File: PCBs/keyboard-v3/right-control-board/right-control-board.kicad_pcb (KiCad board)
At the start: 2 copper layers, 105 x 44 mm, 0 parts

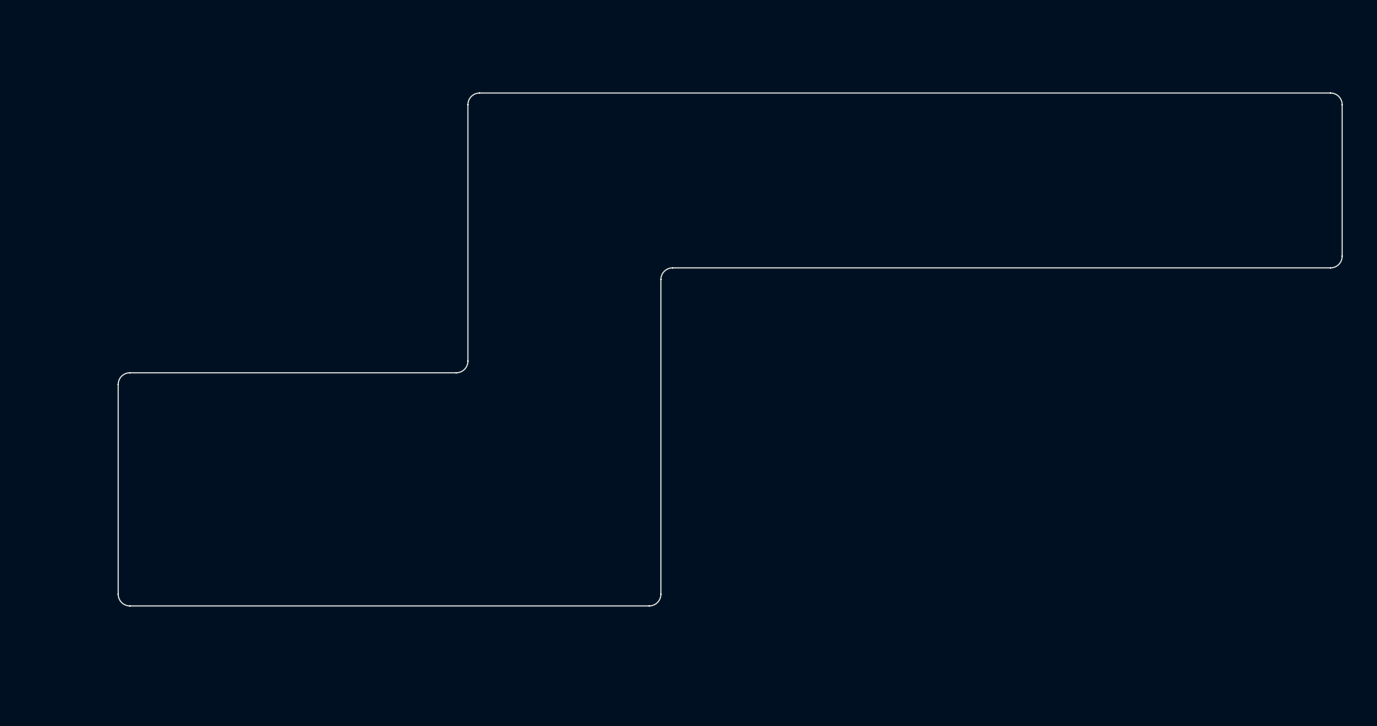
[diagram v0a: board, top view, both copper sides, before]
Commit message: Updated right-control-board layout
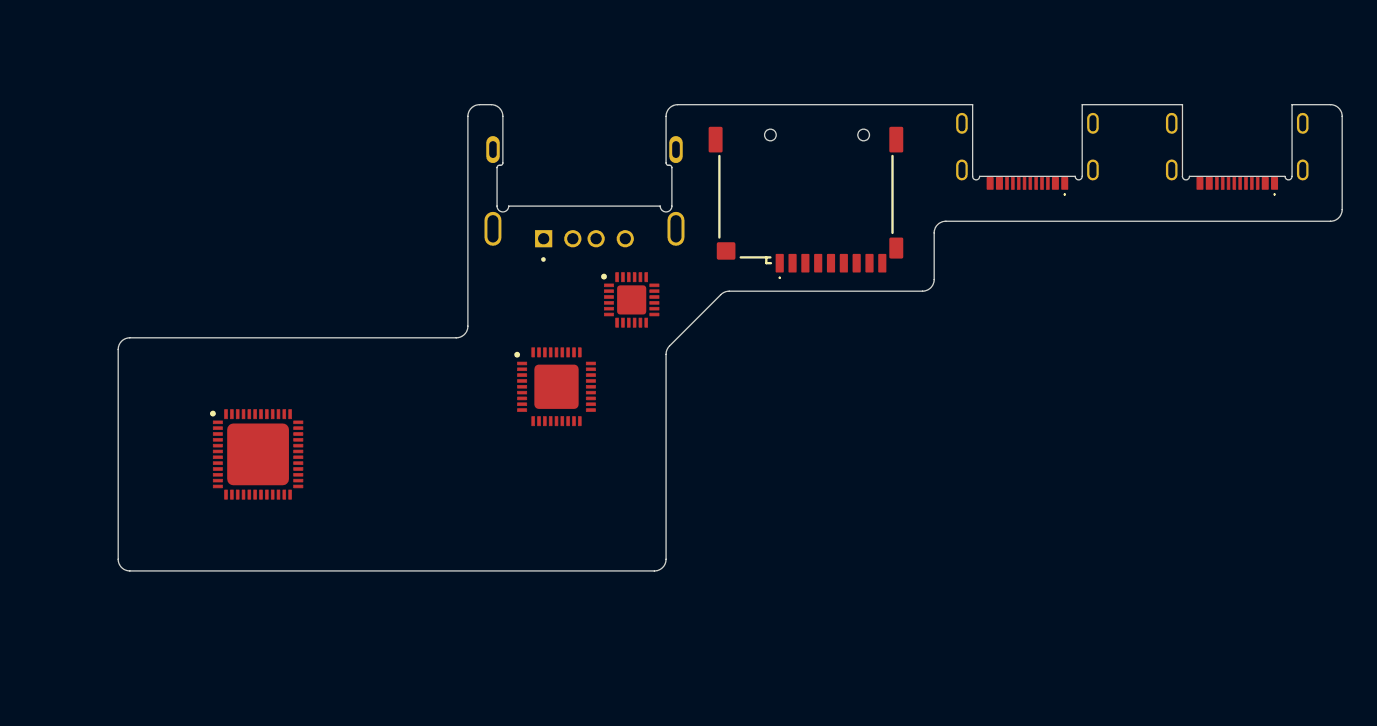
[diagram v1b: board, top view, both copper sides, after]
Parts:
- added J101: USB4510-03-1-A, project_footprints:USB4510031A, F.Cu at (196.0, 78.0)
- added J102: USB4510-03-1-A, project_footprints:USB4510031A, F.Cu at (178.0, 78.0)
- added J103: GSB12J21C1EU, project_footprints:GSB12J21C1EU, F.Cu at (140.0, 79.0)
- added J105: MSD-1-A, project_footprints:MSD1A, F.Cu at (159.0, 84.5)
- added U101: USB2534-1080AEN, project_footprints:QFN50P600X600X100-37N-D, F.Cu at (137.6, 102.2)
- added U102: STM32G0C1CEUx, project_footprints:QFN50P700X700X60-49N-D, F.Cu at (112.0, 108.0)
- added U103: GL835, project_footprints:QFN50P400X400X100-25N-D, F.Cu at (144.1, 94.8)
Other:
- board size 105 x 44 mm -> 105 x 40 mm

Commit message: Right control board schematic almost done
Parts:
- added C101: 1u, project_footprints:C_0402, F.Cu at (173.8, 102.2)
- added C102: 10p, project_footprints:C_0402, F.Cu at (173.8, 104.2)
- added C103: 10p, project_footprints:C_0402, F.Cu at (173.8, 106.1)
- added C105: 1u, project_footprints:C_0402, F.Cu at (173.8, 108.1)
- added C106: 100n, project_footprints:C_0402, F.Cu at (173.8, 110.1)
- added C109: 100n, project_footprints:C_0402, F.Cu at (163.3, 116.4)
- added C110: 1u, project_footprints:C_0402, F.Cu at (163.3, 118.4)
- added C111: 4u7, project_footprints:C_0402, F.Cu at (163.3, 120.4)
- added C201: 4u7, project_footprints:C_0402, F.Cu at (184.4, 114.0)
- added C202: 4u7, project_footprints:C_0402, F.Cu at (184.4, 116.0)
- added C203: 22p, project_footprints:C_0402, F.Cu at (184.4, 118.0)
- added C204: 4u7, project_footprints:C_0402, F.Cu at (184.4, 119.9)
- added C205: 4u7, project_footprints:C_0402, F.Cu at (184.4, 121.9)
- added C206: 4u7, project_footprints:C_0402, F.Cu at (184.4, 123.9)
- added C301: 100n, project_footprints:C_0402, F.Cu at (173.8, 114.0)
- added C302: 4u7, project_footprints:C_0402, F.Cu at (173.8, 116.0)
- added C303: 4u7, project_footprints:C_0402, F.Cu at (173.8, 118.0)
- added C304: 100n, project_footprints:C_0402, F.Cu at (176.7, 114.0)
- added C305: 4u7, project_footprints:C_0402, F.Cu at (176.7, 116.0)
- added C306: 100n, project_footprints:C_0402, F.Cu at (176.7, 118.0)
- added C307: 100n, project_footprints:C_0402, F.Cu at (179.6, 114.0)
- added C308: 4u7, project_footprints:C_0402, F.Cu at (179.6, 116.0)
- added C309: 4u7, project_footprints:C_0402, F.Cu at (179.6, 118.0)
- added FL301: EMIF06-MSD02N16, project_footprints:EMIF06MSD02N16, F.Cu at (176.5, 121.1)
- added J501: Conn_02x08_Odd_Even, Connector_PinSocket_1.27mm:PinSocket_2x08_P1.27mm_Horizontal, F.Cu at (97.8, 103.5)
- added L201: 78438313015, project_footprints:L_Wurth_WE-MAIA-1610, F.Cu at (187.6, 122.1)
- added R101: 10k, project_footprints:R_0402, F.Cu at (166.2, 116.4)
- added R102: 10k, project_footprints:R_0402, F.Cu at (166.2, 118.4)
- added R103: 12k, project_footprints:R_0402, F.Cu at (176.7, 102.2)
- added R104: 100k, project_footprints:R_0402, F.Cu at (176.7, 104.2)
- added R105: 47k, project_footprints:R_0402, F.Cu at (176.7, 106.2)
- added R108: 10k, project_footprints:R_0402, F.Cu at (176.7, 108.2)
- added R201: 5k1, project_footprints:R_0402, F.Cu at (170.2, 103.1)
- added R202: 5k1, project_footprints:R_0402, F.Cu at (170.2, 105.1)
- added R203: 5k1, project_footprints:R_0402, F.Cu at (170.2, 107.1)
- added R204: 5k1, project_footprints:R_0402, F.Cu at (170.2, 109.1)
- added R701: 820k, project_footprints:R_0402, F.Cu at (187.3, 114.0)
- added R702: 182k, project_footprints:R_0402, F.Cu at (187.3, 116.0)
- added U104: USBLC6-4SC6, Package_TO_SOT_SMD:SOT-23-6, F.Cu at (186.8, 103.6)
- added U201: USBLC6-4SC6, Package_TO_SOT_SMD:SOT-23-6, F.Cu at (186.8, 108.2)
- added U701: TPS62290TDRVRQ1, project_footprints:SON65P200X200X80-7N, F.Cu at (187.8, 118.8)
- added Y101: CX2016SA24000D0HLLG3, Crystal:Crystal_SMD_2016-4Pin_2.0x1.6mm, F.Cu at (180.2, 103.0)
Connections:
- J101 pad A1: Net-(J101-GND-PadA1) -> GND
- J101 pad A12: Net-(J101-GND-PadA1) -> GND
- J101 pad A4: Net-(J101-VBUS-PadA4) -> VBUS
- J101 pad A5: unconnected-(J101-CC1-PadA5) -> /USB Connectors/USB0_CC1
- J101 pad A6: Net-(J101-D+-PadA6) -> /USB Connectors/USB0.DP
- J101 pad A7: Net-(J101-D--PadA7) -> /USB Connectors/USB0.DN
- J101 pad A9: Net-(J101-VBUS-PadA4) -> VBUS
- J101 pad B5: unconnected-(J101-CC2-PadB5) -> /USB Connectors/USB0_CC2
- J101 pad B6: Net-(J101-D+-PadA6) -> /USB Connectors/USB0.DP
- J101 pad B7: Net-(J101-D--PadA7) -> /USB Connectors/USB0.DN
- J101 pad MH1: Net-(J101-PadMH1) -> GND
- J101 pad MH2: Net-(J101-PadMH1) -> GND
- J101 pad MH3: Net-(J101-PadMH1) -> GND
- J101 pad MH4: Net-(J101-PadMH1) -> GND
- J102 pad A1: Net-(J102-GND-PadA1) -> GND
- J102 pad A12: Net-(J102-GND-PadA1) -> GND
- J102 pad A4: Net-(J102-VBUS-PadA4) -> VBUS
- J102 pad A5: unconnected-(J102-CC1-PadA5) -> /USB Connectors/USB1_CC1
- J102 pad A6: Net-(J102-D+-PadA6) -> /USB Connectors/USB1.DP
- J102 pad A7: Net-(J102-D--PadA7) -> /USB Connectors/USB1.DN
- J102 pad A9: Net-(J102-VBUS-PadA4) -> VBUS
- J102 pad B5: unconnected-(J102-CC2-PadB5) -> /USB Connectors/USB1_CC2
- J102 pad B6: Net-(J102-D+-PadA6) -> /USB Connectors/USB1.DP
- J102 pad B7: Net-(J102-D--PadA7) -> /USB Connectors/USB1.DN
- J102 pad MH1: Net-(J102-PadMH1) -> GND
- J102 pad MH2: Net-(J102-PadMH1) -> GND
- J102 pad MH3: Net-(J102-PadMH1) -> GND
- J102 pad MH4: Net-(J102-PadMH1) -> GND
- J103 pad 1: unconnected-(J103-VCC-Pad1) -> VBUS
- J103 pad 2: unconnected-(J103-D--Pad2) -> /USB Connectors/USB2.DP
- J103 pad 3: unconnected-(J103-D+-Pad3) -> /USB Connectors/USB2.DN
- J103 pad 4: unconnected-(J103-GND-Pad4) -> GND
- J103 pad SH1: Net-(J103-SHIELD-PadSH1) -> GND
- J103 pad SH2: Net-(J103-SHIELD-PadSH1) -> GND
- J103 pad SH3: Net-(J103-SHIELD-PadSH1) -> GND
- J103 pad SH4: Net-(J103-SHIELD-PadSH1) -> GND
- J105 pad 1: unconnected-(J105-DAT2-Pad1) -> /SD Card/SD_D2_EX
- J105 pad 10: Net-(J105-SHIELD-Pad10) -> GND
- J105 pad 11: Net-(J105-SHIELD-Pad10) -> GND
- J105 pad 12: Net-(J105-SHIELD-Pad10) -> GND
- J105 pad 2: unconnected-(J105-CD/DAT3-Pad2) -> /SD Card/SD_D3_EX
- J105 pad 3: unconnected-(J105-CMD-Pad3) -> /SD Card/SD_CMD_EX
- J105 pad 4: unconnected-(J105-VDD-Pad4) -> /SD Card/SD_VCC
- J105 pad 5: unconnected-(J105-CLK-Pad5) -> /SD Card/SD_CLK_EX
- J105 pad 6: unconnected-(J105-VSS-Pad6) -> GND
- J105 pad 7: unconnected-(J105-DAT0-Pad7) -> /SD Card/SD_D0_EX
- J105 pad 8: unconnected-(J105-DAT1-Pad8) -> /SD Card/SD_D1_EX
- J105 pad 9: Net-(J105-SHIELD-Pad10) -> GND
- J105 pad CD: unconnected-(J105-PadCD) -> /SD Card/CD
- U101 pad 1: unconnected-(U101-SWAP_USBDN1_DM/PRT_DIS_M1-Pad1) -> /USB Connectors/USB1.DN
- U101 pad 10: unconnected-(U101-VDDA33_1-Pad10) -> +3V3
- U101 pad 14: unconnected-(U101-VDDCR12-Pad14) -> +1V2
- U101 pad 15: unconnected-(U101-VDD33_1-Pad15) -> +3V3
- U101 pad 2: unconnected-(U101-SWAP_USBDN1_DP/PRT_DIS_P1-Pad2) -> /USB Connectors/USB1.DP
- U101 pad 22: unconnected-(U101-SDA/SMBDATA/NON_REM1-Pad22) -> /MCU/SDA
- U101 pad 23: unconnected-(U101-VDD33_2-Pad23) -> +3V3
- U101 pad 24: unconnected-(U101-SCL/SMBCLK/CFG_SEL0-Pad24) -> /MCU/SCL
- U101 pad 25: unconnected-(U101-HS_IND/CFG_SEL1-Pad25) -> /USB Hub/CFG_SEL1
- U101 pad 26: unconnected-(U101-RESET_N-Pad26) -> /Daughter Board Connectors/~{KEYS_RST}
- U101 pad 27: unconnected-(U101-VBUS_DET-Pad27) -> /USB Hub/VBUS_DET
- U101 pad 29: unconnected-(U101-VDDA33_2-Pad29) -> +3V3
- U101 pad 3: unconnected-(U101-USBDN2_DM/PRT_DIS_M2-Pad3) -> /USB Connectors/USB2.DN
- U101 pad 30: unconnected-(U101-FLEX_USBUP_DM-Pad30) -> /USB Connectors/USB0.DN
- U101 pad 31: unconnected-(U101-FLEX_USBUP_DP-Pad31) -> /USB Connectors/USB0.DP
- U101 pad 32: unconnected-(U101-XTAL2-Pad32) -> /USB Hub/XTAL2
- U101 pad 33: unconnected-(U101-XTAL1/REFCLK-Pad33) -> /USB Hub/XTAL1
- U101 pad 35: unconnected-(U101-RBIAS-Pad35) -> /USB Hub/RBIAS
- U101 pad 36: unconnected-(U101-VDDA33_3-Pad36) -> +3V3
- U101 pad 37: unconnected-(U101-VSS-Pad37) -> GND
- U101 pad 4: unconnected-(U101-USBDN2_DP/PRT_DIS_P2-Pad4) -> /USB Connectors/USB2.DP
- U101 pad 6: unconnected-(U101-USBDN3_DM/PRT_DIS_M3-Pad6) -> /SD Card/DN
- U101 pad 7: unconnected-(U101-USBDN3_DP/PRT_DIS_P3-Pad7) -> /SD Card/DP
- U101 pad 8: unconnected-(U101-USBDN4_DM/PRT_DIS_M4-Pad8) -> /MCU/DN
- U101 pad 9: unconnected-(U101-USBDN4_DP/PRT_DIS_P4-Pad9) -> /MCU/DP
- U102 pad 10: unconnected-(U102-PF2-Pad10) -> /Daughter Board Connectors/~{KEYS_RST}
- U102 pad 33: unconnected-(U102-PA9/PA11-Pad33) -> /MCU/DN
- U102 pad 34: unconnected-(U102-PA10/PA12-Pad34) -> /MCU/DP
- U102 pad 35: unconnected-(U102-PA13-Pad35) -> /Debug Connector/CTRL.SWDIO
- U102 pad 36: unconnected-(U102-PA14-Pad36) -> /Debug Connector/CTRL.SWCLK
- U102 pad 4: unconnected-(U102-VBAT-Pad4) -> +3V3
- U102 pad 47: unconnected-(U102-PB8-Pad47) -> /MCU/SCL
- U102 pad 48: unconnected-(U102-PB9-Pad48) -> /MCU/SDA
- U102 pad 49: Net-(U102-VSS-Pad49) -> GND
- U102 pad 5: unconnected-(U102-VREF+-Pad5) -> /MCU/VREF+
- U102 pad 6: unconnected-(U102-VDD-Pad6) -> +3V3
- U102 pad 7: Net-(U102-VSS-Pad49) -> GND
- U103 pad 1: unconnected-(U103-VDD-Pad1) -> /SD Card/VDD
- U103 pad 10: unconnected-(U103-SD_CDZ-Pad10) -> /SD Card/CD
- U103 pad 11: unconnected-(U103-SD_WP-Pad11) -> GND
- U103 pad 12: unconnected-(U103-SD_D1-Pad12) -> /SD Card/SD_D1
- U103 pad 13: unconnected-(U103-SD_D0-Pad13) -> /SD Card/SD_D0
- U103 pad 16: unconnected-(U103-SDREG-Pad16) -> /SD Card/SDREG
- U103 pad 18: unconnected-(U103-SD_CLK-Pad18) -> /SD Card/SD_CLK
- U103 pad 20: unconnected-(U103-SD_CMD-Pad20) -> /SD Card/SD_CMD
- U103 pad 22: unconnected-(U103-SD_D3-Pad22) -> /SD Card/SD_D3
- U103 pad 23: unconnected-(U103-SD_D2-Pad23) -> /SD Card/SD_D2
- U103 pad 25: unconnected-(U103-EP-Pad25) -> GND
- U103 pad 3: unconnected-(U103-DM-Pad3) -> /SD Card/DP
- U103 pad 4: unconnected-(U103-DP-Pad4) -> /SD Card/DN
- U103 pad 5: unconnected-(U103-A3V3-Pad5) -> +3V3
- U103 pad 6: unconnected-(U103-D3V3-Pad6) -> +3V3
- U103 pad 7: unconnected-(U103-SD_VCC-Pad7) -> /SD Card/SD_VCC
- U103 pad 9: unconnected-(U103-PIO5-Pad9) -> GND
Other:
- board size 105 x 40 mm -> 110.9 x 40 mm

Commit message: Key board schematic done and layout half done
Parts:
- added J601: F31Z1A7H111008, project_footprints:F31Z1A7H111008, F.Cu at (123.5, 114.6)
- added J602: F31Z1A7H111008, project_footprints:F31Z1A7H111008, F.Cu at (107.5, 114.6)
- moved U201 54.4 mm to (134.0, 95.0), turned to 90 degrees
- moved FL301 40.9 mm to (145.0, 95.0), turned to -90 degrees
- moved U104 17.6 mm to (187.0, 86.0), turned to 180 degrees
- moved U101 5.23 mm to (134.0, 106.0)
- moved U103 4.06 mm to (140.0, 95.0), turned to -90 degrees
- moved U102 3.61 mm to (115.0, 106.0)

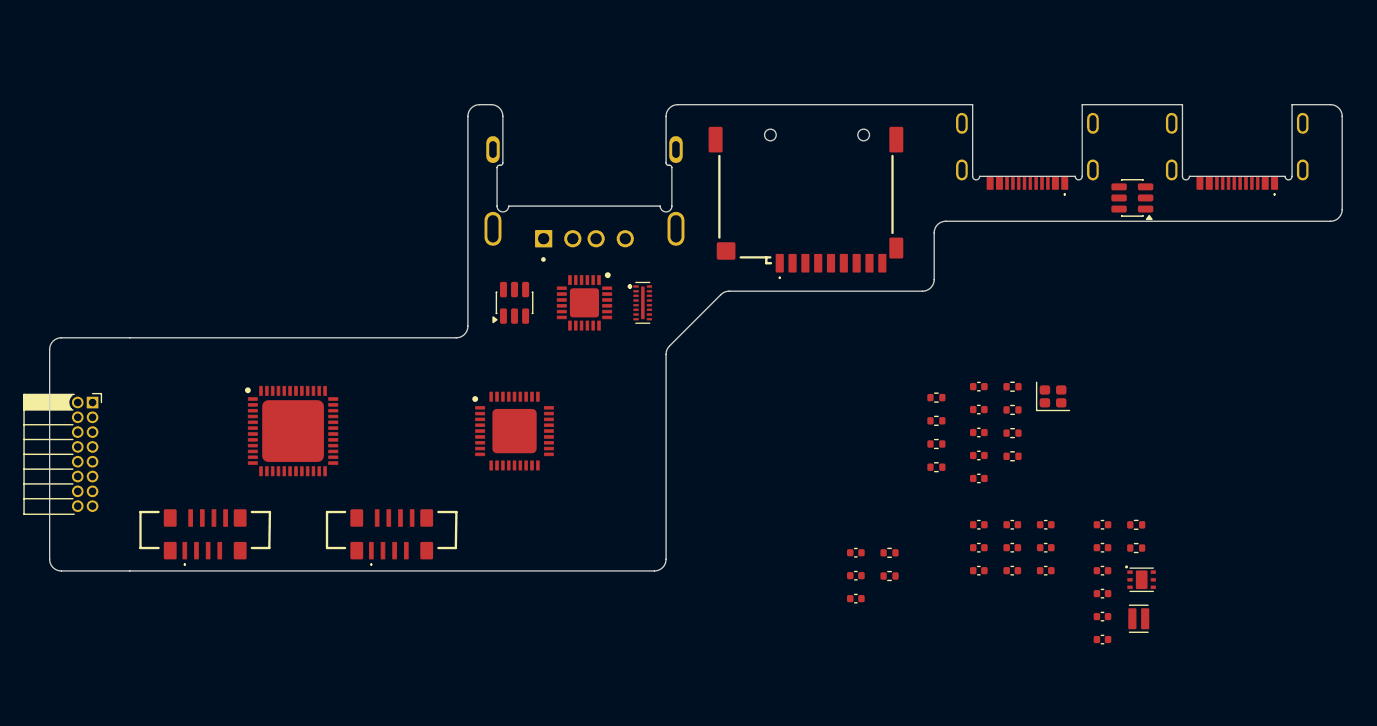
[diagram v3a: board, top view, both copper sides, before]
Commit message: Added debug-breakout board, progress on right side schematics & layout
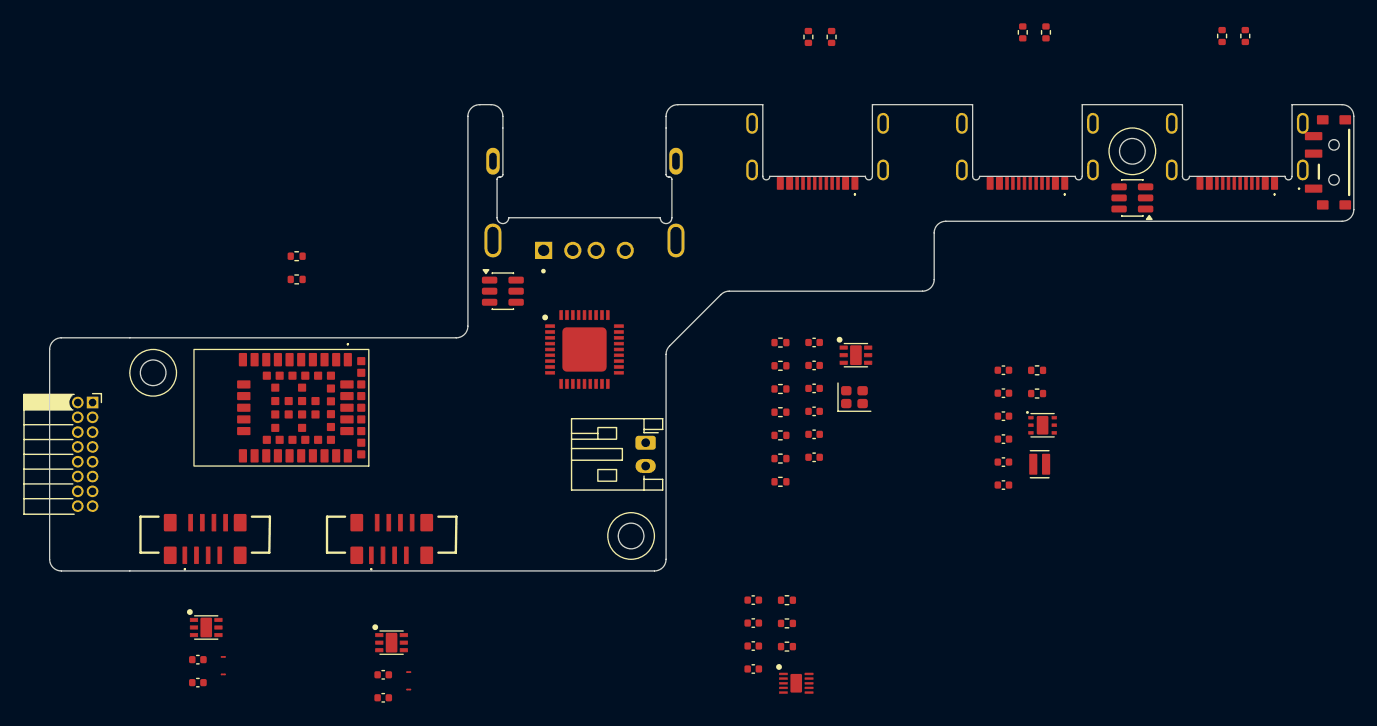
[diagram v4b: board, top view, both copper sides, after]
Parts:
- removed C109, C301, C304, C306, C307: 100n, project_footprints:C_0402
- removed C110: 1u, project_footprints:C_0402
- removed C111, C302, C303, C305, C308, C309: 4u7, project_footprints:C_0402
- removed FL301: EMIF06-MSD02N16, project_footprints:EMIF06MSD02N16
- removed J105: MSD-1-A, project_footprints:MSD1A
- removed R201, R202, R204: 5k1, project_footprints:R_0402
- removed U102: STM32G0C1CEUx, project_footprints:QFN50P700X700X60-49N-D
- removed U103: GL835, project_footprints:QFN50P400X400X100-25N-D
- added C601: 1u, project_footprints:C_0402, F.Cu at (122.7, 126.9)
- added C602: 1u, project_footprints:C_0402, F.Cu at (106.8, 125.6)
- added C603: 1u, project_footprints:C_0402, F.Cu at (106.8, 127.6)
- added C604: 1u, project_footprints:C_0402, F.Cu at (122.7, 128.9)
- added C701: 4u7, project_footprints:C_0402, F.Cu at (154.5, 120.5)
- added C702: 4u7, project_footprints:C_0402, F.Cu at (154.5, 122.5)
- added C703: 1u, project_footprints:C_0402, F.Cu at (154.5, 124.4)
- added C704: 1u, project_footprints:C_0402, F.Cu at (154.5, 126.4)
- added C801: 1u, project_footprints:C_0402, F.Cu at (159.7, 108.2)
- added H101: MountingHole, MountingHole:MountingHole_2.2mm_M2, F.Cu at (187.0, 82.0)
- added H102: MountingHole, MountingHole:MountingHole_2.2mm_M2, F.Cu at (144.0, 115.0)
- added H103: MountingHole, MountingHole:MountingHole_2.2mm_M2, F.Cu at (103.0, 101.0)
- added J201: USB4510-03-1-A, project_footprints:USB4510031A, F.Cu at (160.0, 78.0)
- added J701: Conn_01x02, Connector_JST:JST_PH_S2B-PH-K_1x02_P2.00mm_Horizontal, F.Cu at (145.2, 107.0)
- added NT601: NetTie_2, project_footprints:NetTie-2_SMD_Pad0.15mm, F.Cu at (124.9, 126.7)
- added NT602: NetTie_2, project_footprints:NetTie-2_SMD_Pad0.15mm, F.Cu at (124.9, 128.2)
- added NT603: NetTie_2, project_footprints:NetTie-2_SMD_Pad0.15mm, F.Cu at (109.0, 125.4)
- added NT604: NetTie_2, project_footprints:NetTie-2_SMD_Pad0.15mm, F.Cu at (109.0, 126.9)
- added R205: 5k1, project_footprints:R_0402, F.Cu at (194.7, 72.1)
- added R206: 5k1, project_footprints:R_0402, F.Cu at (196.7, 72.1)
- added R208: 22k, project_footprints:R_0402, F.Cu at (177.6, 71.8)
- added R209: 22k, project_footprints:R_0402, F.Cu at (161.2, 72.2)
- added R210: 22k, project_footprints:R_0402, F.Cu at (159.2, 72.2)
- added R401: 2M, project_footprints:R_0402, F.Cu at (115.3, 91.0)
- added R402: 806k, project_footprints:R_0402, F.Cu at (115.3, 93.0)
- added R703: 1k, project_footprints:R_0402, F.Cu at (157.4, 120.5)
- added R704: 13k, project_footprints:R_0402, F.Cu at (157.4, 122.5)
- added R705: 10k, project_footprints:R_0402, F.Cu at (157.4, 124.5)
- added R801: 10k, project_footprints:R_0402, F.Cu at (156.8, 110.3)
- added S701: PCM12SMTBR, project_footprints:PCM12SMTBR, F.Cu at (204.3, 83.0)
- added U401: NINA-B302-00B, project_footprints:NINAB30200B, F.Cu at (114.0, 104.0)
- added U601: NCP380HMU05AATBG, project_footprints:SON65P200X200X55-7N, F.Cu at (123.5, 124.2)
- added U602: NCP380HMU05AATBG, project_footprints:SON65P200X200X55-7N, F.Cu at (107.5, 122.8)
- added U702: BQ25185DLHR, project_footprints:SON40P220X200X80-11N, F.Cu at (158.2, 127.6)
- added U801: NCP380HMU05AATBG, project_footprints:SON65P200X200X55-7N, F.Cu at (163.3, 99.5)
- R203: value 5k1 -> 22k
- moved R203 36.5 mm to (179.6, 71.8), turned to -90 degrees
- moved R101 20.3 mm to (156.8, 98.4)
- moved R102 20.3 mm to (156.8, 100.4)
- moved R103 19.9 mm to (156.8, 102.4)
- moved R104 19.9 mm to (156.8, 104.4)
- moved R105 19.9 mm to (156.8, 106.4)
- moved R108 19.9 mm to (156.8, 108.4)
- moved Y101 17.0 mm to (163.2, 103.1)
- moved C205 15.7 mm to (175.9, 108.7)
- moved C206 15.7 mm to (175.9, 110.6)
- moved C201 15.7 mm to (175.9, 100.8)
- moved C202 15.7 mm to (175.9, 102.8)
- moved C203 15.7 mm to (175.9, 104.7)
- moved C204 15.7 mm to (175.9, 106.7)
- moved L201 15.7 mm to (179.1, 108.8)
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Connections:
- C105 pad 1: +3V3 -> +3V3_USB
- C106 pad 1: +3V3 -> +3V3_USB
- C201 pad 1: VBUS -> +VSYS
- C202 pad 1: VBUS -> +VSYS
- J103 pad 2: /USB Connectors/USB2.DP -> /USB Connectors/USB3.DP
- J103 pad 3: /USB Connectors/USB2.DN -> /USB Connectors/USB3.DN
- J501 pad 1: unconnected-(J501-Pin_1-Pad1) -> /Debug Connector/CTRL.SWCLK
- J501 pad 10: unconnected-(J501-Pin_10-Pad10) -> /Daughter Board Connectors/KEYS.SWDIO
- J501 pad 11: unconnected-(J501-Pin_11-Pad11) -> GND
- J501 pad 12: unconnected-(J501-Pin_12-Pad12) -> /Debug Connector/KEYS.RX
- J501 pad 13: unconnected-(J501-Pin_13-Pad13) -> /Daughter Board Connectors/~{KEYS_RST}
- J501 pad 14: unconnected-(J501-Pin_14-Pad14) -> GND
- J501 pad 15: unconnected-(J501-Pin_15-Pad15) -> +3V3
- J501 pad 16: unconnected-(J501-Pin_16-Pad16) -> VBUS
- J501 pad 2: unconnected-(J501-Pin_2-Pad2) -> /Debug Connector/CTRL.SWDIO
- J501 pad 3: unconnected-(J501-Pin_3-Pad3) -> GND
- J501 pad 4: unconnected-(J501-Pin_4-Pad4) -> GND
- J501 pad 5: unconnected-(J501-Pin_5-Pad5) -> /Daughter Board Connectors/KNOB.SWCLK
- J501 pad 6: unconnected-(J501-Pin_6-Pad6) -> /Daughter Board Connectors/KNOB.SWDIO
- J501 pad 7: unconnected-(J501-Pin_7-Pad7) -> GND
- J501 pad 8: unconnected-(J501-Pin_8-Pad8) -> /Debug Connector/KNOB.RX
- J501 pad 9: unconnected-(J501-Pin_9-Pad9) -> /Daughter Board Connectors/KEYS.SWCLK
- J601 pad 1: unconnected-(J601-Pad1) -> /Daughter Board Connectors/~{KEYS_RST}
- J601 pad 2: unconnected-(J601-Pad2) -> /Daughter Board Connectors/KNOB_SWDIO/~{KNOB_INT}
- J601 pad 3: unconnected-(J601-Pad3) -> /Daughter Board Connectors/KNOB.SWCLK
- J601 pad 4: unconnected-(J601-Pad4) -> GND
- J601 pad 5: unconnected-(J601-Pad5) -> /Daughter Board Connectors/KNOB.TX
- J601 pad 6: unconnected-(J601-Pad6) -> /Daughter Board Connectors/KNOB.RX
- J601 pad 7: unconnected-(J601-Pad7) -> +3V3
- J601 pad 8: unconnected-(J601-Pad8) -> /Daughter Board Connectors/KNOB_5V
- J602 pad 1: unconnected-(J602-Pad1) -> /Daughter Board Connectors/~{KEYS_RST}
- J602 pad 2: unconnected-(J602-Pad2) -> /Daughter Board Connectors/KEYS_SWDIO/~{INT}
- J602 pad 3: unconnected-(J602-Pad3) -> /Daughter Board Connectors/KEYS.SWCLK
- J602 pad 4: unconnected-(J602-Pad4) -> GND
- J602 pad 5: unconnected-(J602-Pad5) -> /Daughter Board Connectors/KEYS.TX
- J602 pad 6: unconnected-(J602-Pad6) -> /Daughter Board Connectors/KEYS.RX
- J602 pad 7: unconnected-(J602-Pad7) -> +3V3
- J602 pad 8: unconnected-(J602-Pad8) -> /Daughter Board Connectors/KEYS_5V
- R101 pad 1: +3V3 -> +3V3_USB
- R102 pad 1: +3V3 -> +3V3_USB
- R108 pad 1: /USB Hub/CFG_SEL1 -> GND
- R108 pad 2: GND -> /USB Hub/CFG_SEL1
- R203 pad 1: /USB Connectors/USB0_CC2 -> VBUS
- R203 pad 2: GND -> /USB Connectors/USB1_CC1
- U101 pad 10: +3V3 -> +3V3_USB
- U101 pad 15: +3V3 -> +3V3_USB
- U101 pad 23: +3V3 -> +3V3_USB
- U101 pad 26: /Daughter Board Connectors/~{KEYS_RST} -> /USB Hub/~{RST}
- U101 pad 29: +3V3 -> +3V3_USB
- U101 pad 36: +3V3 -> +3V3_USB
- U101 pad 6: /SD Card/DN -> /USB Connectors/USB3.DN
- U101 pad 7: /SD Card/DP -> /USB Connectors/USB3.DP
- U104 pad 4: unconnected-(U104-I/O3-Pad4) -> /USB Connectors/USB1.DP
- U104 pad 6: unconnected-(U104-I/O4-Pad6) -> /USB Connectors/USB1.DN
- U201 pad 1: /USB Connectors/USB1.DP -> /USB Connectors/USB2.DP
- U201 pad 3: /USB Connectors/USB1.DN -> /USB Connectors/USB2.DN
- U201 pad 4: /USB Connectors/USB2.DP -> /USB Connectors/USB3.DP
- U201 pad 6: /USB Connectors/USB2.DN -> /USB Connectors/USB3.DN
- U701 pad 2: VBUS -> GND
- U701 pad 4: VBUS -> Net-(S701-COM)
- U701 pad 5: VBUS -> +VSYS
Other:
- board size 110.9 x 40 mm -> 111.9 x 40 mm
